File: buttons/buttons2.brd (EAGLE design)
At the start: 69 x 44 mm, 14 parts

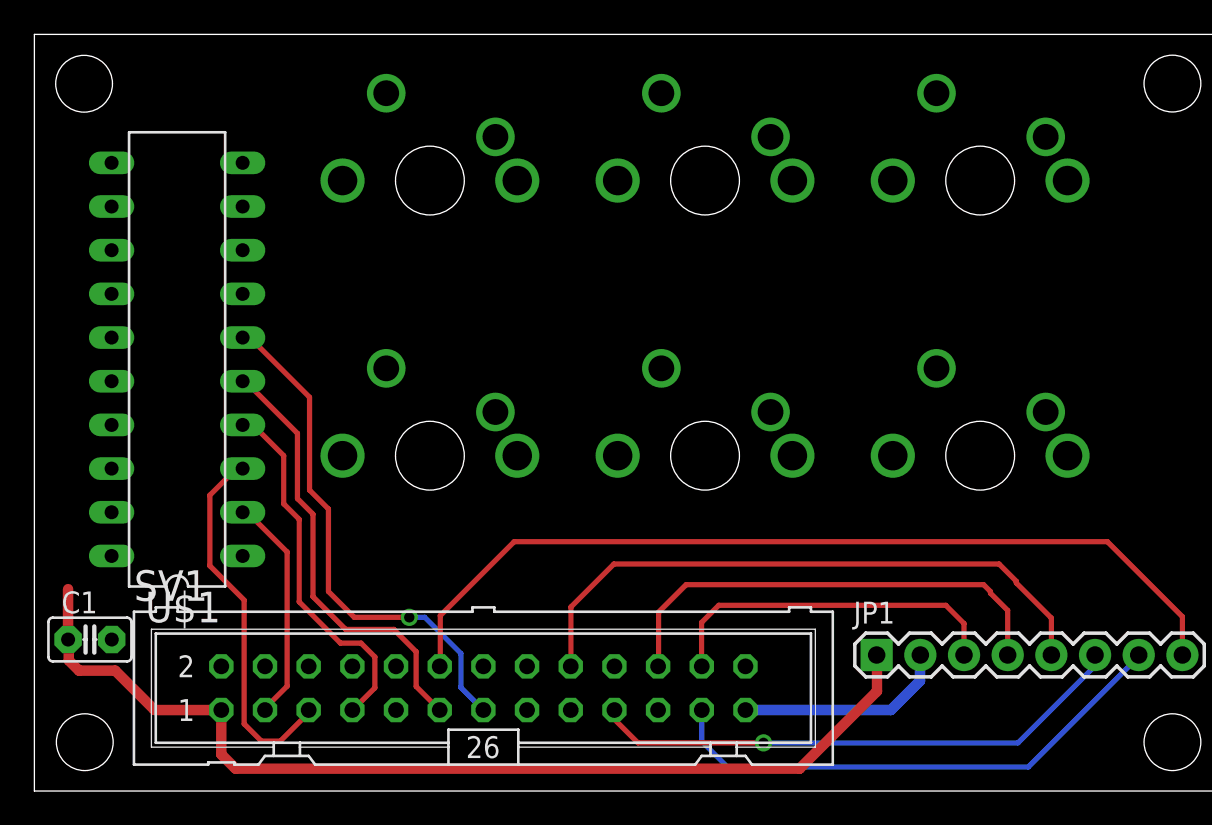
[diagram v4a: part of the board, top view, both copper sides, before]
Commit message: routed all signals
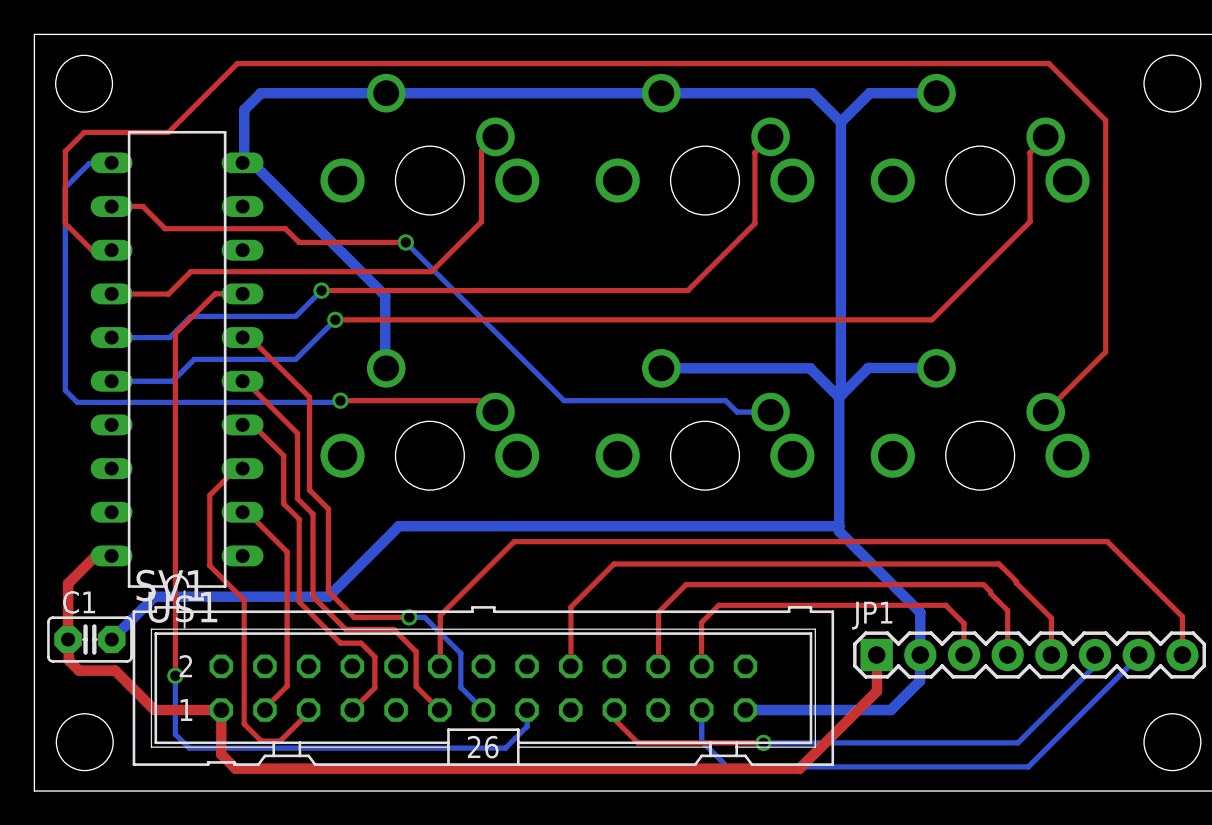
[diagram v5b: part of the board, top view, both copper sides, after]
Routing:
- net GND: track 12.4 -> 169.1 mm
- net N$4: track 0.00 -> 89.9 mm
- net N$1: track 0.00 -> 62.6 mm, vias 0 -> 1
- net BUTTON6: track 0.00 -> 50.4 mm, vias 0 -> 1
- net N$2: track 0.00 -> 45.6 mm, vias 0 -> 1
- net N$5: track 0.00 -> 43.3 mm, vias 0 -> 1
- net N$6: track 0.00 -> 40.9 mm, vias 0 -> 1
- net N$3: track 0.00 -> 28.5 mm
- net VCC: track 59.3 -> 62.8 mm

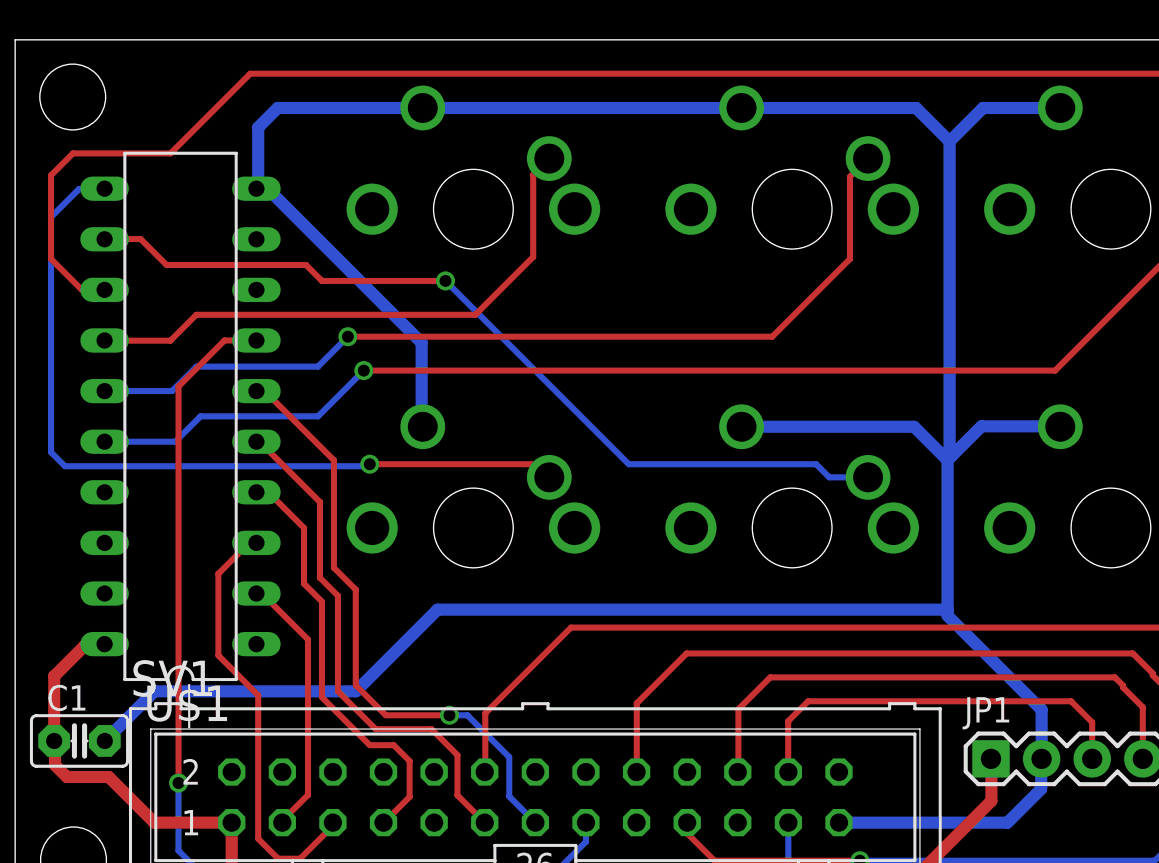
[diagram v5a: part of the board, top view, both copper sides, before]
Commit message: more work on button PCB, but not done
Problem is that the buttons need to be rotated
180 degrees!  Because the board will be flipped,
the top of the PCB will be towards the bottom
of the top plate of the enclosure.  Duh.
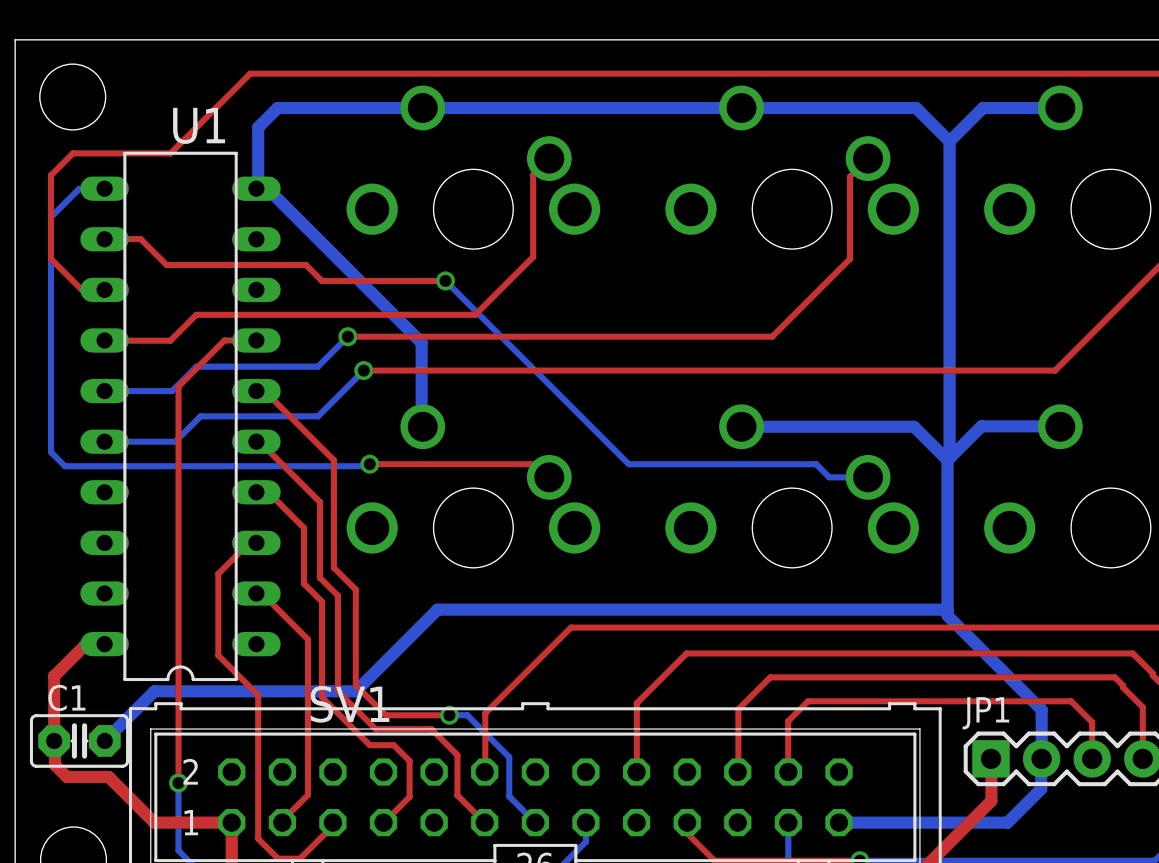
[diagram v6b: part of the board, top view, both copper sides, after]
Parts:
- U1: value TINY2313-*P* -> attiny2313
- renumbered U$1 to U1
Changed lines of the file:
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@@
 </autorouter>
 <elements>
-<element name="SV1" library="con-harting-ml" package="ML26" value="RPi_GPIO" x="26.11" y="5.98">
+<element name="SV1" library="con-harting-ml" package="ML26" value="RPi_GPIO" x="26.11" y="5.98" smashed="yes">
 <attribute name="OC_NEWARK" value="unknown" x="60.4" y="-24.5" size="1.778" layer="27" display="off"/>
 <attribute name="MPN" value="" x="60.4" y="-24.5" size="1.778" layer="27" display="off"/>
 <attribute name="MF" value="" x="60.4" y="-24.5" size="1.778" layer="27" display="off"/>
 <attribute name="OC_FARNELL" value="unknown" x="60.4" y="-24.5" size="1.778" layer="27" display="off"/>
+<attribute name="NAME" x="14.69" y="9.76" size="1.778" layer="25" font="vector" ratio="10"/>
+<attribute name="VALUE" x="27.08" y="9.76" size="1.778" layer="27" font="vector" ratio="10"/>
 </element>
-<element name="JP1" library="SparkFun-Connectors" package="1X08" value="LCD_CONN" x="48.98" y="7.91"/>
-<element name="C1" library="capacitor-wima" package="C2.5-2" value="0.1uF" x="3.23" y="8.81"/>
+<element name="JP1" library="SparkFun-Connectors" package="1X08" value="LCD_CONN" x="48.98" y="7.91" smashed="yes">
+<attribute name="NAME" x="47.6338" y="9.7388" size="1.27" layer="25" font="vector" ratio="10"/>
+<attribute name="VALUE" x="47.71" y="4.735" size="1.27" layer="27" font="vector"/>
+</element>
+<element name="C1" library="capacitor-wima" package="C2.5-2" value="0.1uF" x="3.23" y="8.81" smashed="yes">
+<attribute name="NAME" x="1.579" y="10.334" size="1.27" layer="25" font="vector" ratio="10"/>
+<attribute name="VALUE" x="0.679" y="6.016" size="1.27" layer="27" font="vector" ratio="10"/>
+</element>
 <element name="STANDOFF1" library="SparkFun-Electromechanical" package="STAND-OFF" value="STAND-OFF" x="66.18" y="2.84"/>
 <element name="STANDOFF2" library="SparkFun-Electromechanical" package="STAND-OFF" value="STAND-OFF" x="2.93" y="2.84"/>
@@
 <element name="S5" library="cherrymx" package="CHERRY-MX-I" value="CHERRY-MX-I" x="39" y="35.5" rot="MR0"/>
 <element name="S6" library="cherrymx" package="CHERRY-MX-I" value="CHERRY-MX-I" x="55" y="35.5" rot="MR0"/>
-<element name="U$1" library="avr-6" package="DIL20" value="TINY2313-*P*" x="8.3" y="25.1" rot="R90"/>
+<element name="U1" library="avr-6" package="DIL20" value="attiny2313" x="8.3" y="25.1" smashed="yes" rot="R90">
+<attribute name="NAME" x="10.74" y="40.5872" size="1.778" layer="25" font="vector" ratio="10" rot="R180"/>
+<attribute name="VALUE" x="8.962" y="18.14" size="1.778" layer="27" font="vector" ratio="10" rot="R90"/>
+</element>
 </elements>
 <signals>
@@
 <contactref element="S2" pad="PIN-2"/>
 <contactref element="S1" pad="PIN-2"/>
-<contactref element="U$1" pad="10"/>
-<contactref element="U$1" pad="10"/>
+<contactref element="U1" pad="10"/>
+<contactref element="U1" pad="10"/>
 <wire x1="41.35" y1="4.71" x2="49.81" y2="4.71" width="0.6096" layer="16"/>
 <wire x1="49.81" y1="4.71" x2="51.5" y2="6.4" width="0.6096" layer="16"/>
@@
 <signal name="N$1">
 <contactref element="S6" pad="PIN-1"/>
-<contactref element="U$1" pad="16"/>
+<contactref element="U1" pad="16"/>
 <wire x1="4.49" y1="23.83" x2="8.03" y2="23.83" width="0.3048" layer="16"/>
 <wire x1="8.03" y1="23.83" x2="9.3" y2="25.1" width="0.3048" layer="16"/>
@@
 <signal name="N$2">
 <contactref element="S5" pad="PIN-1"/>
-<contactref element="U$1" pad="15"/>
+<contactref element="U1" pad="15"/>
 <wire x1="42.81" y1="38.04" x2="41.9" y2="37.13" width="0.3048" layer="1"/>
 <wire x1="41.9" y1="37.13" x2="41.9" y2="33" width="0.3048" layer="1"/>
@@
 <signal name="N$3">
 <contactref element="S4" pad="PIN-1"/>
-<contactref element="U$1" pad="14"/>
+<contactref element="U1" pad="14"/>
 <wire x1="26.81" y1="38.04" x2="26" y2="37.23" width="0.3048" layer="1"/>
 <wire x1="26" y1="37.23" x2="26" y2="33.1" width="0.3048" layer="1"/>
@@
 <signal name="N$4">
 <contactref element="S3" pad="PIN-1"/>
-<contactref element="U$1" pad="13"/>
+<contactref element="U1" pad="13"/>
 <wire x1="58.81" y1="22.04" x2="62.3" y2="25.53" width="0.3048" layer="1"/>
 <wire x1="62.3" y1="25.53" x2="62.3" y2="39" width="0.3048" layer="1"/>
@@
 <signal name="N$5">
 <contactref element="S2" pad="PIN-1"/>
-<contactref element="U$1" pad="12"/>
+<contactref element="U1" pad="12"/>
 <wire x1="42.81" y1="22.04" x2="40.86" y2="22.04" width="0.3048" layer="16"/>
 <wire x1="40.86" y1="22.04" x2="40.2" y2="22.7" width="0.3048" layer="16"/>
@@
 <signal name="N$6">
 <contactref element="S1" pad="PIN-1"/>
-<contactref element="U$1" pad="11"/>
+<contactref element="U1" pad="11"/>
 <wire x1="4.49" y1="36.53" x2="4.57" y2="36.53" width="0.3048" layer="16"/>
 <wire x1="4.57" y1="36.53" x2="4.6" y2="36.5" width="0.3048" layer="16"/>
@@
 <contactref element="JP1" pad="1"/>
 <contactref element="SV1" pad="1"/>
-<contactref element="U$1" pad="20"/>
-<contactref element="U$1" pad="20"/>
+<contactref element="U1" pad="20"/>
+<contactref element="U1" pad="20"/>
 <wire x1="1.96" y1="8.81" x2="1.96" y2="12.06" width="0.6096" layer="1"/>
 <wire x1="11.7" y1="1.3" x2="44.5" y2="1.3" width="0.6096" layer="1"/>
@@
 <signal name="BUTTON1">
 <contactref element="SV1" pad="3"/>
-<contactref element="U$1" pad="2"/>
+<contactref element="U1" pad="2"/>
 <wire x1="14.7" y1="13.9" x2="14.7" y2="6.1" width="0.3048" layer="1"/>
 <wire x1="14.7" y1="6.1" x2="13.41" y2="4.81" width="0.3048" layer="1"/>
@@
 <signal name="BUTTON2">
 <contactref element="SV1" pad="5"/>
-<contactref element="U$1" pad="3"/>
+<contactref element="U1" pad="3"/>
 <wire x1="15.95" y1="4.85" x2="15.95" y2="4.71" width="0.3048" layer="1"/>
 <wire x1="15.95" y1="4.71" x2="15.95" y2="4.55" width="0.3048" layer="1"/>
@@
 <signal name="BUTTON3">
 <contactref element="SV1" pad="7"/>
-<contactref element="U$1" pad="4"/>
+<contactref element="U1" pad="4"/>
 <wire x1="19.8" y1="6" x2="18.51" y2="4.71" width="0.3048" layer="1"/>
 <wire x1="18.51" y1="4.71" x2="18.49" y2="4.71" width="0.3048" layer="1"/>
@@
 <signal name="BUTTON4">
 <contactref element="SV1" pad="11"/>
-<contactref element="U$1" pad="5"/>
+<contactref element="U1" pad="5"/>
 <wire x1="15.3" y1="20.8" x2="15.3" y2="17" width="0.3048" layer="1"/>
 <wire x1="15.3" y1="17" x2="16.2" y2="16.1" width="0.3048" layer="1"/>
@@
 <signal name="BUTTON5">
 <contactref element="SV1" pad="13"/>
-<contactref element="U$1" pad="6"/>
+<contactref element="U1" pad="6"/>
 <wire x1="16" y1="22.9" x2="16" y2="17.5" width="0.3048" layer="1"/>
 <wire x1="16" y1="17.5" x2="17.1" y2="16.4" width="0.3048" layer="1"/>
@@
 <signal name="BUTTON6">
 <contactref element="SV1" pad="15"/>
-<contactref element="U$1" pad="7"/>
+<contactref element="U1" pad="7"/>
 <wire x1="28.65" y1="4.71" x2="28.65" y2="3.75" width="0.3048" layer="16"/>
 <wire x1="28.65" y1="3.75" x2="27.4" y2="2.5" width="0.3048" layer="16"/>

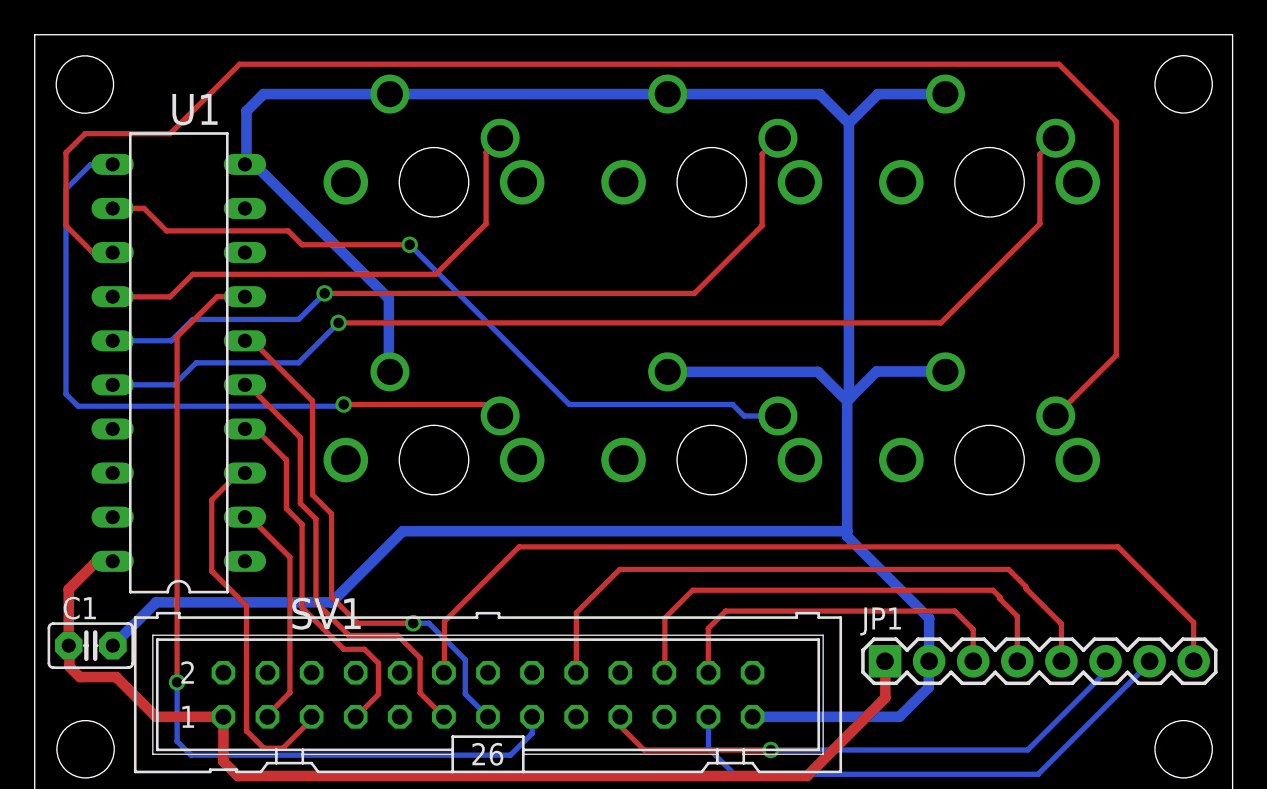
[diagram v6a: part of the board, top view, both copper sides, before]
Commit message: more or less complete PCB for Cherry MX switches
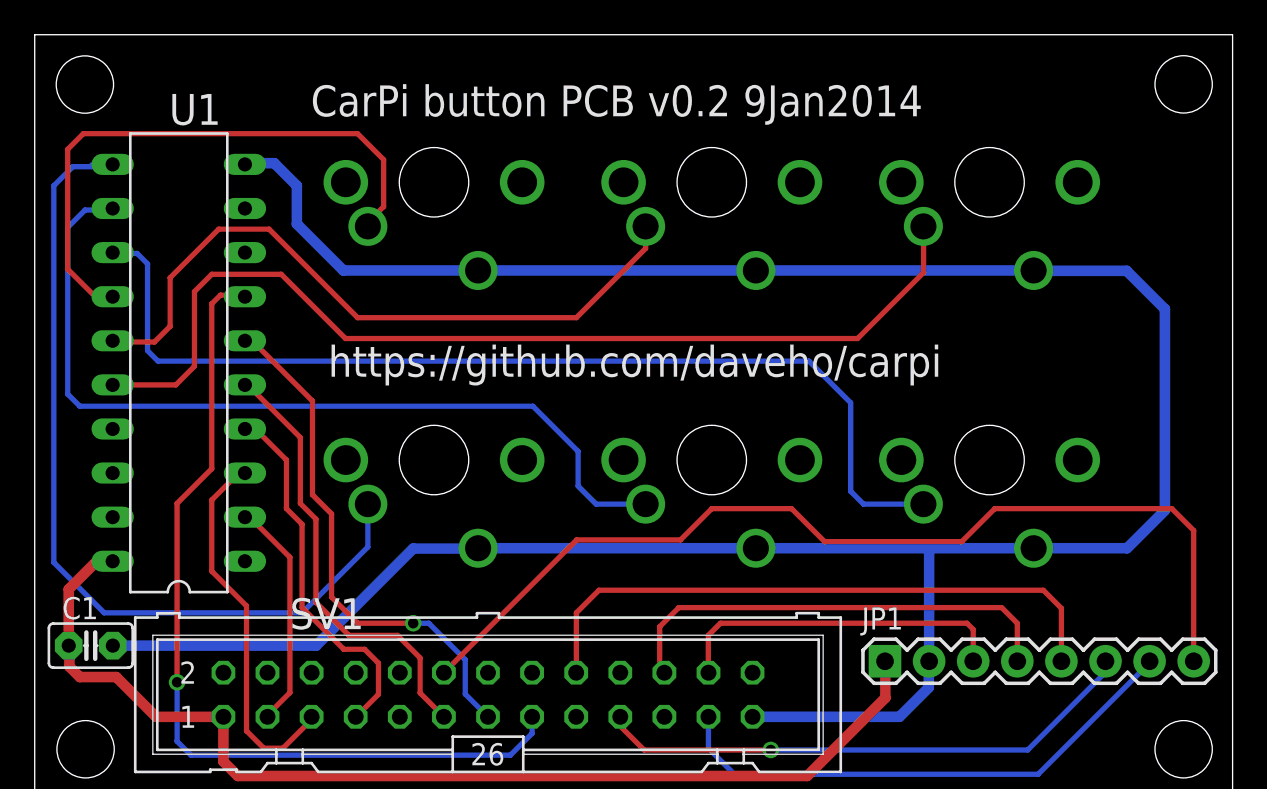
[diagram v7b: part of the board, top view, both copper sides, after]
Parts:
- turned S1 to 180 degrees
- turned S2 to 180 degrees
- turned S3 to 180 degrees
- turned S4 to 180 degrees
- turned S5 to 180 degrees
- turned S6 to 180 degrees
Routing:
- net N$4: track 89.9 -> 58.6 mm
- net GND: track 169.1 -> 152.1 mm
- net N$6: track 40.9 -> 49.0 mm, vias 1 -> 0
- net N$5: track 43.3 -> 49.7 mm, vias 1 -> 0
- net N$2: track 45.6 -> 40.1 mm, vias 1 -> 0
- net N$3: track 28.5 -> 33.6 mm
- net N$1: track 62.6 -> 57.6 mm, vias 1 -> 0
- net LED: track 51.9 -> 56.7 mm
- net RESET: track 27.4 -> 26.4 mm
- net CS: track 20.5 -> 19.7 mm
- net DC: track 35.9 -> 35.4 mm
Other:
- board text added: "CarPi button PCB v0.2 9Jan2014"
- board text added: "https://github.com/daveho/carpi"
